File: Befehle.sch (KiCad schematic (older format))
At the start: 60 parts, among them J1 2PinTerminalBlocktg, J2 2PinTerminalBlocktg, J3 3PinTerminalBlocktg, J4 2PinTerminalBlocktg, J5 2PinTerminalBlocktg, P1 CONN_02X10, P2 CONN_02X10, U1 74LS14, U2 74540, U3 7400, U4 74HCT02, U5 74LS541, U6 74LS373, U7 74LS139, U8 74LS540

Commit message: wires gelegt und schamdoozels beseitigt
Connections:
- net labels added: d44, v1, v2
- net labels removed: 11, d0, d8
- wire segments 285 -> 289
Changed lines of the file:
@@
 d1
 Text Label -6300 4700 3    60   ~ 0
-d2
+d3
 Text Label -6400 4700 3    60   ~ 0
-d3
+d5
 Text Label -6500 4700 3    60   ~ 0
 d4
 Text Label -6600 4700 3    60   ~ 0
-d5
+d6
 Text Label -6700 4700 3    60   ~ 0
-d6
+d44
 Text Label -6800 4700 3    60   ~ 0
 d7
 Text Label -7100 4400 1    60   ~ 0
-d1
+d7
 Text Label -7100 4600 1    60   ~ 0
 d2
 Text Label -6950 5000 1    60   ~ 0
-d3
+d6
 Text Label -7050 5150 1    60   ~ 0
-d4
+d44
 Text Label -7100 5500 1    60   ~ 0
 d5
 Text Label -7100 5700 1    60   ~ 0
-d6
+d4
 Text Label -7100 6050 1    60   ~ 0
-d7
+d1
 Text Label -7100 6250 1    60   ~ 0
-d8
+d3
 Entry Wire Line
 	-5900 6800 -6000 6900
@@
 d1
 Text Label -6100 6900 1    60   ~ 0
-d2
+d7
 Text Label -6200 6900 1    60   ~ 0
 d3
 Text Label -6300 6900 1    60   ~ 0
-d4
+d44
 Text Label -6400 6900 1    60   ~ 0
 d5
@@
 d6
 Text Label -6600 6900 1    60   ~ 0
-d7
+d4
 Text Label -6200 550  1    60   ~ 0
 y1
@@
 	0    -1   -1   0
 $EndComp
-Text Label -6950 6250 0    60   ~ 0
-11
 Text Label -6900 4700 1    60   ~ 0
 d2
@@
 F 0 "D22" V 2841 6822 50  0000 R CNN
 F 1 "D" V 2750 6822 50  0000 R CNN
-F 2 "Diodes_ThroughHole:D_DO-41_SOD81_P10.16mm_Horizontal" V 2659 6822 50  0000 R CNN
+F 2 "Diodes_ThroughHole:D_DO-41_SOD81_P10.16mm_Horizontal" V 2650 6750 50  0000 R CNN
 F 3 "" H 2750 6900 50  0000 C CNN
 	1    2750 6900
@@
 Wire Wire Line
 	-8700 7850 -8700 8100
-Connection ~ -8700 7850
 Wire Wire Line
 	-9350 5350 -9150 5350
@@
 	37900 55900 37900 44500
 Wire Bus Line
-	37900 44500 50200 44500
-Wire Bus Line
-	50200 44500 50200 20050
-Wire Bus Line
-	50200 20050 65050 20050
-Wire Bus Line
-	65050 45000 77600 45000
-Wire Bus Line
 	77600 45000 77600 54250
 Wire Bus Line
 	77600 54250 77700 54250
-Wire Bus Line
-	65050 20050 65050 45000
-Wire Bus Line
-	56650 20400 56650 27200
-Wire Bus Line
-	64850 27200 64850 26900
-Wire Bus Line
-	50250 27200 56650 27200
-Connection ~ 56650 27200
 Wire Bus Line
 	-54500 -26200 -54500 -18100
@@
 	-3900 5450 -3900 6050
 Wire Wire Line
-	-8700 7850 -8200 7850
-Wire Wire Line
 	-9150 5350 -8650 5350
 Wire Wire Line
@@
 	-5450 -800 -5450 -550
 Wire Wire Line
-	-8300 5050 -8300 6650
-Wire Bus Line
-	56650 27200 64850 27200
+	-8300 5050 -8300 5600
 Wire Bus Line
 	-54500 -18100 -40100 -18100
@@
 Connection ~ -6500 3300
 Text Label -5900 6900 1    60   ~ 0
-d0
+d2
+Connection ~ -8300 5600
+Wire Wire Line
+	-8300 5600 -8300 6150
+Connection ~ -8300 6150
+Wire Wire Line
+	-8300 6150 -8300 6650
+Text Label -8650 6650 0    50   ~ 0
+v1
+Text Label -8400 7850 0    50   ~ 0
+v1
+Connection ~ -8700 7850
+Wire Wire Line
+	-8700 7850 -8400 7850
+Wire Wire Line
+	-8400 7850 -8200 7850
+Text Label -8400 7850 0    50   ~ 0
+v2
+Text Label -8750 5450 0    50   ~ 0
+v2
+Wire Wire Line
+	-8300 6650 -8500 6650
 Wire Bus Line
 	-6500 6800 -6300 6800
 Wire Bus Line
+	-4650 1950 -3950 1950
+Wire Bus Line
+	-6900 2650 -3950 2650
+Wire Bus Line
+	-6300 4850 -6300 6800
+Wire Bus Line
 	-6300 6800 -5800 6800
 Wire Bus Line
-	-4650 1950 -3950 1950
-Wire Bus Line
-	-6900 2650 -3950 2650
-Wire Bus Line
-	-6300 4850 -6300 6800
-Wire Bus Line
 	-7050 4850 -6300 4850
+Connection ~ -8300 6650
+Connection ~ -8500 6650
 $EndSCHEMATC

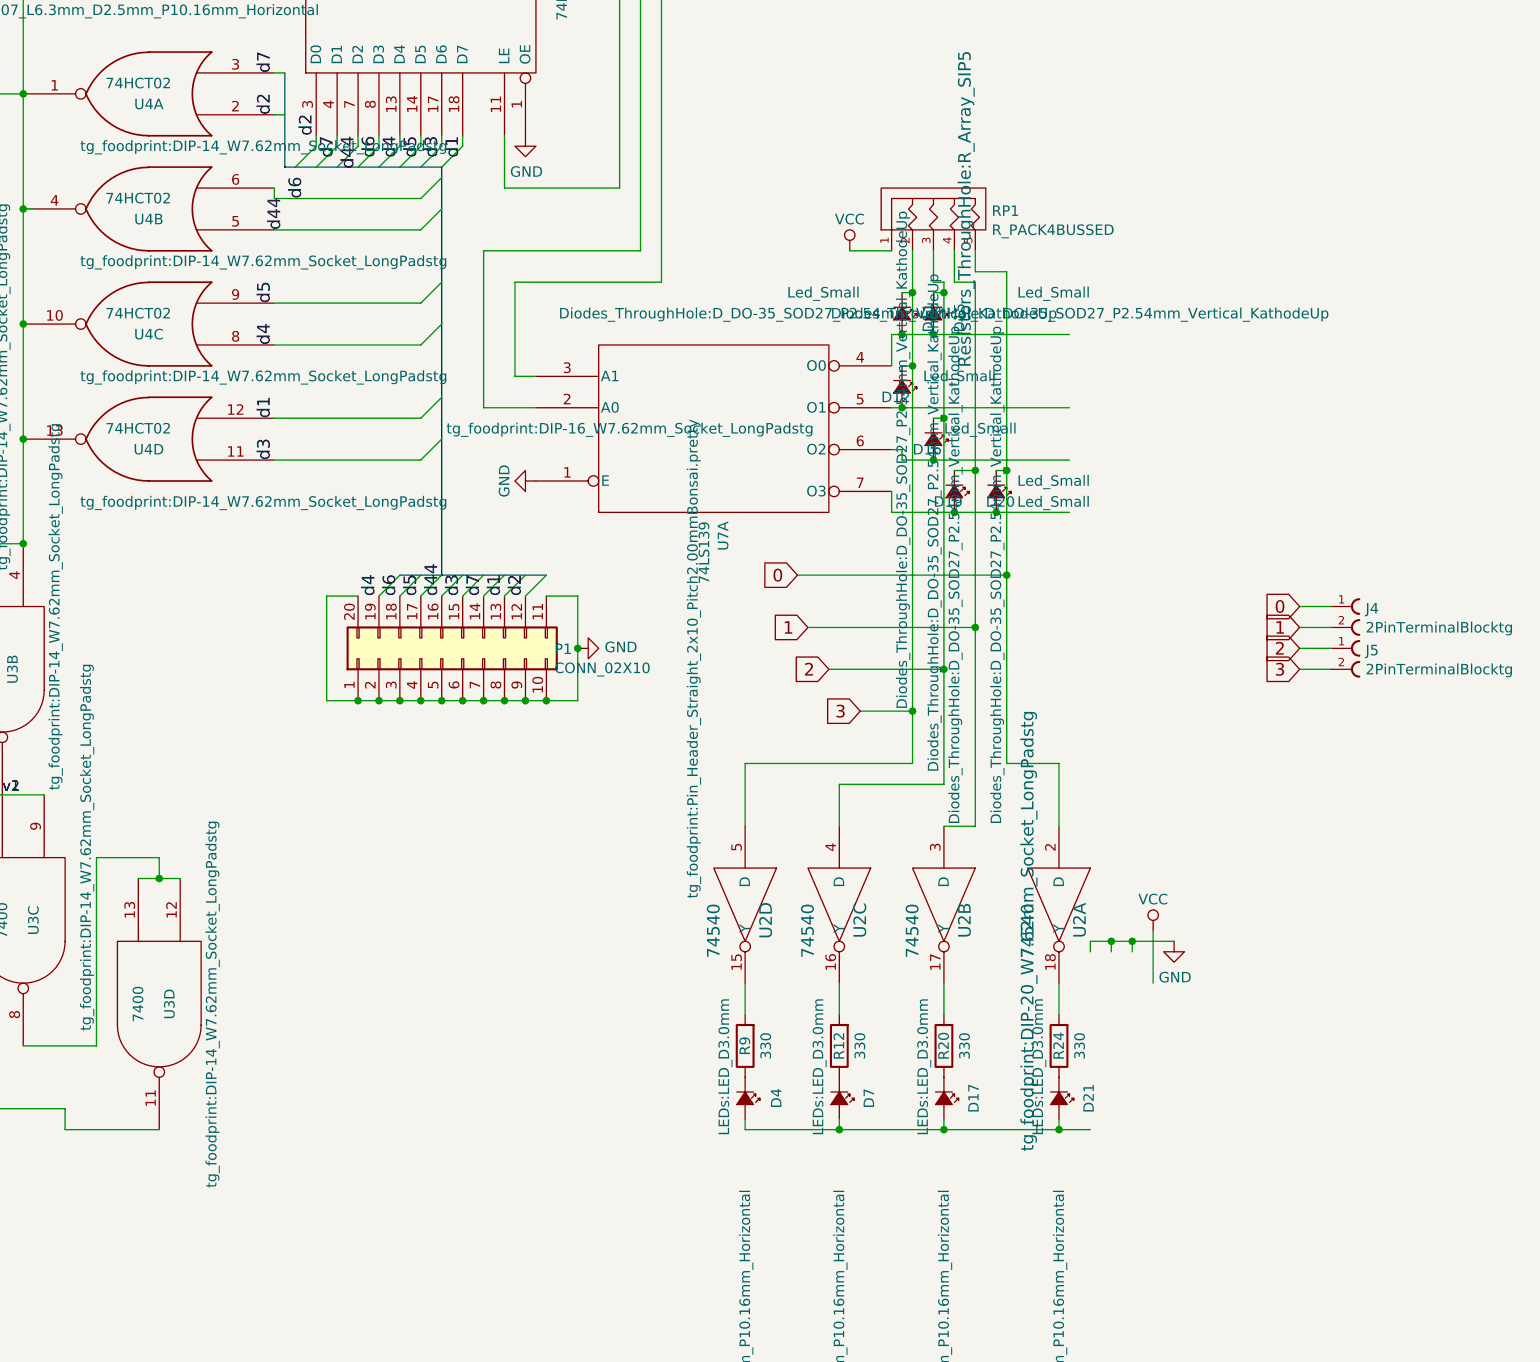
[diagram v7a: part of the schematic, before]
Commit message: wires gelegt footprints getauscht
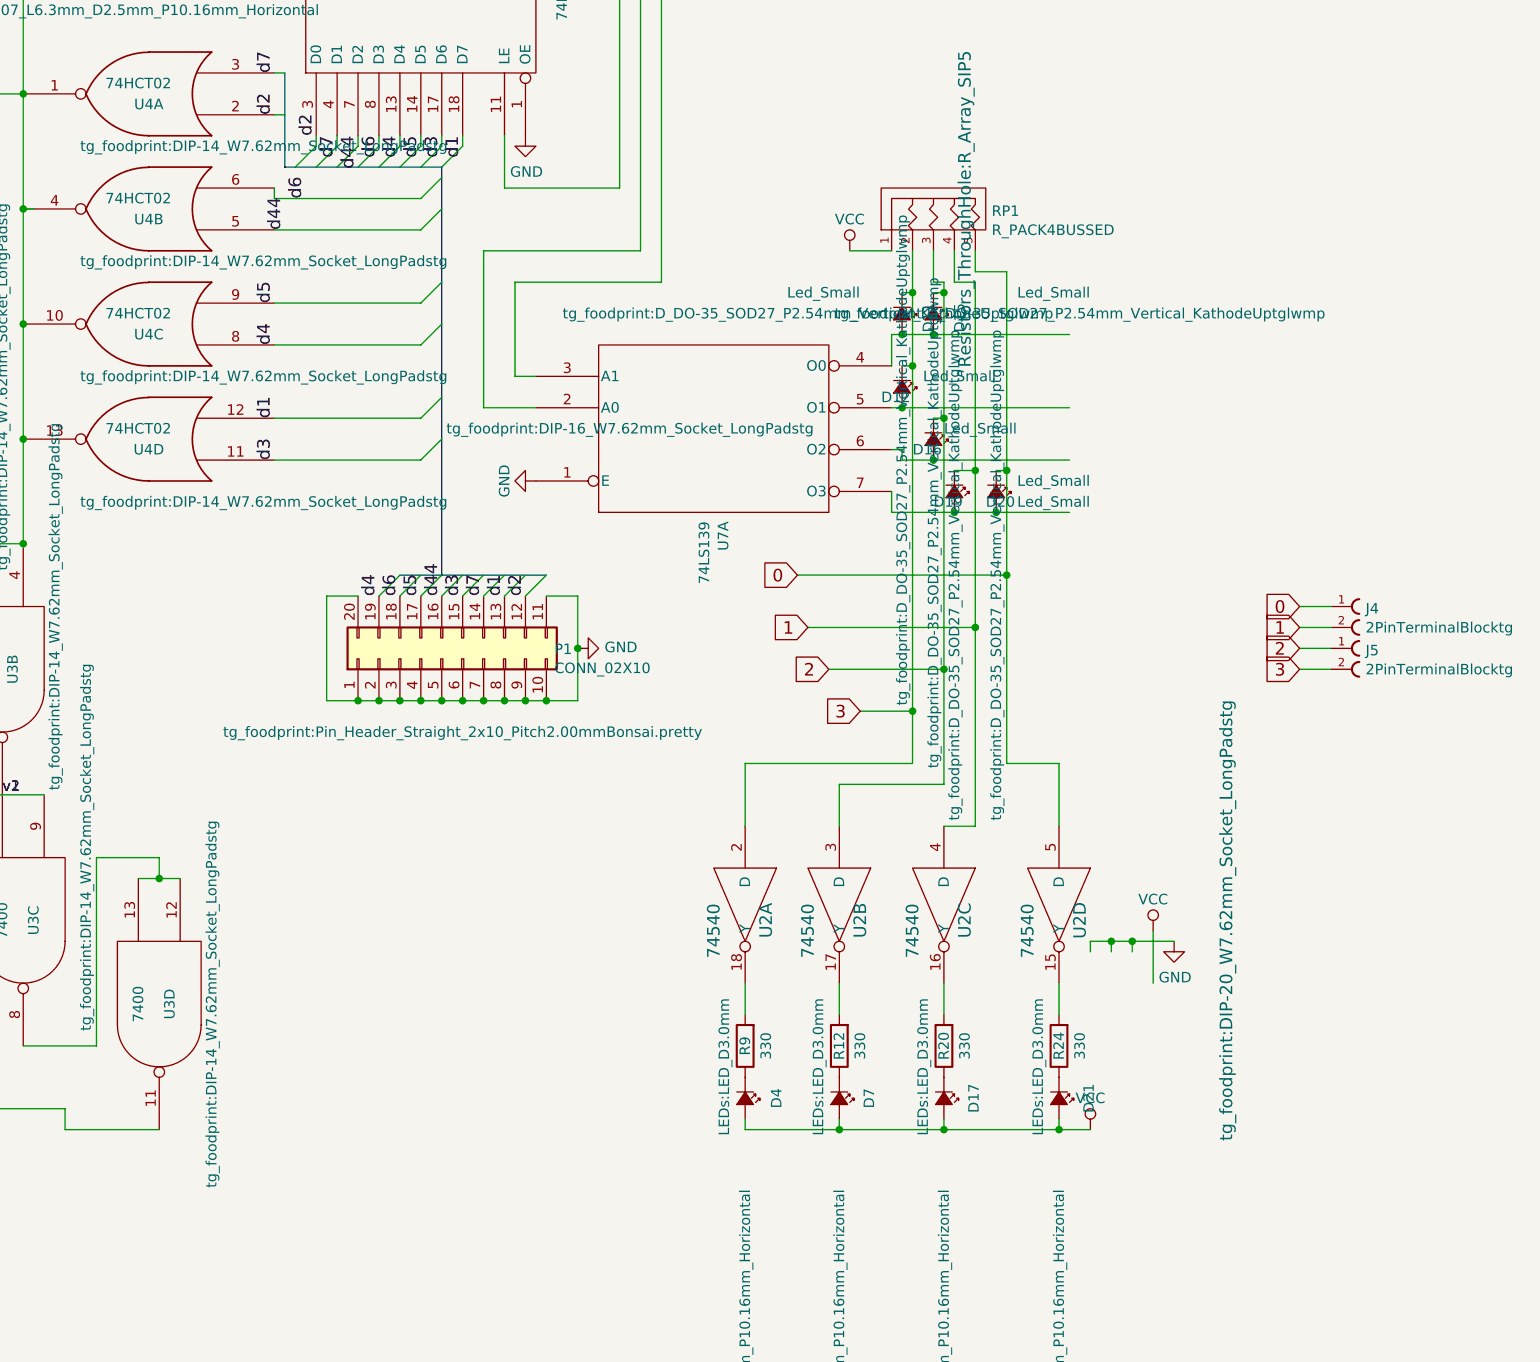
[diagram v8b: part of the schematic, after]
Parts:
- D11, D12, D15, D16, D19, D20: footprint Diodes_ThroughHole:D_DO-35_SOD27_P2.54mm_Vertical_KathodeUp -> tg_foodprint:D_DO-35_SOD27_P2.54mm_Vertical_KathodeUptglwmp
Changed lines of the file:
@@
 F 0 "D15" H -4000 5675 50  0000 L CNN
 F 1 "Led_Small" V -4050 5950 50  0000 L CNN
-F 2 "Diodes_ThroughHole:D_DO-35_SOD27_P2.54mm_Vertical_KathodeUp" V -3950 6250 50  0000 C CNN
+F 2 "tg_foodprint:D_DO-35_SOD27_P2.54mm_Vertical_KathodeUptglwmp" V -3950 6250 50  0000 C CNN
 F 3 "" V -3950 5550 50  0000 C CNN
 	1    -3950 5550
@@
 F 0 "D11" H -4150 5675 50  0000 L CNN
 F 1 "Led_Small" V -4200 5000 50  0000 L CNN
-F 2 "Diodes_ThroughHole:D_DO-35_SOD27_P2.54mm_Vertical_KathodeUp" V -4100 5100 50  0000 C CNN
+F 2 "tg_foodprint:D_DO-35_SOD27_P2.54mm_Vertical_KathodeUptglwmp" V -4100 5100 50  0000 C CNN
 F 3 "" V -4100 5550 50  0000 C CNN
 	1    -4100 5550
@@
 F 0 "D12" V -4050 5800 50  0000 L CNN
 F 1 "Led_Small" V -4150 6000 50  0000 L CNN
-F 2 "Diodes_ThroughHole:D_DO-35_SOD27_P2.54mm_Vertical_KathodeUp" H -3750 5900 50  0000 C CNN
+F 2 "tg_foodprint:D_DO-35_SOD27_P2.54mm_Vertical_KathodeUptglwmp" H -3750 5900 50  0000 C CNN
 F 3 "" V -4100 5900 50  0000 C CNN
 	1    -4100 5900
@@
 F 0 "D16" V -3900 6050 50  0000 L CNN
 F 1 "Led_Small" V -4000 6200 50  0000 L CNN
-F 2 "Diodes_ThroughHole:D_DO-35_SOD27_P2.54mm_Vertical_KathodeUp" H -3550 6150 50  0000 C CNN
+F 2 "tg_foodprint:D_DO-35_SOD27_P2.54mm_Vertical_KathodeUptglwmp" H -3550 6150 50  0000 C CNN
 F 3 "" V -3950 6150 50  0000 C CNN
 	1    -3950 6150
@@
 F 0 "D20" V -3600 6350 50  0000 L CNN
 F 1 "Led_Small" V -3700 6500 50  0000 L CNN
-F 2 "Diodes_ThroughHole:D_DO-35_SOD27_P2.54mm_Vertical_KathodeUp" H -3250 6400 50  0000 C CNN
+F 2 "tg_foodprint:D_DO-35_SOD27_P2.54mm_Vertical_KathodeUptglwmp" H -3250 6400 50  0000 C CNN
 F 3 "" V -3650 6400 50  0000 C CNN
 	1    -3650 6400
@@
 F 0 "D19" V -3800 6300 50  0000 L CNN
 F 1 "Led_Small" V -3800 6700 50  0000 L CNN
-F 2 "Diodes_ThroughHole:D_DO-35_SOD27_P2.54mm_Vertical_KathodeUp" H -3450 6400 50  0000 C CNN
+F 2 "tg_foodprint:D_DO-35_SOD27_P2.54mm_Vertical_KathodeUptglwmp" H -3450 6400 50  0000 C CNN
 F 3 "" V -3850 6400 50  0000 C CNN
 	1    -3850 6400
@@
 F 0 "P1" V -6254 6662 50  0000 R CNN
 F 1 "CONN_02X10" V -6345 6662 50  0000 R CNN
-F 2 "tg_foodprint:Pin_Header_Straight_2x10_Pitch2.00mmBonsai.pretty" H -6300 6000 50  0000 C CNN
+F 2 "tg_foodprint:Pin_Header_Straight_2x10_Pitch2.00mmBonsai.pretty" V -6650 7100 50  0000 C CNN
 F 3 "" H -6300 6000 50  0000 C CNN
 	1    -6300 7200
@@
 $Comp
 L 74540:74540 U2
-U 4 1 5A28303B
+U 1 1 5A28303B
 P -4850 8350
 F 0 "U2" H -4750 8450 60  0000 C CNN
@@
 F 2 "tg_foodprint:DIP-20_W7.62mm_Socket_LongPadstg" H -4700 8200 60  0001 C CNN
 F 3 "" H -4700 8200 60  0001 C CNN
-	4    -4850 8350
+	1    -4850 8350
 	0    1    1    0
 $EndComp
 $Comp
 L 74540:74540 U2
-U 3 1 5A282F54
+U 2 1 5A282F54
 P -4400 8350
 F 0 "U2" H -4300 8450 60  0000 C CNN
@@
 F 2 "tg_foodprint:DIP-20_W7.62mm_Socket_LongPadstg" H -4250 8200 60  0001 C CNN
 F 3 "" H -4250 8200 60  0001 C CNN
-	3    -4400 8350
+	2    -4400 8350
 	0    1    1    0
 $EndComp
 $Comp
 L 74540:74540 U2
-U 2 1 5A282E5F
+U 3 1 5A282E5F
 P -3900 8350
 F 0 "U2" H -3800 8450 60  0000 C CNN
@@
 F 2 "Housings_DIP:DIP-20_W7.62mm_Socket_LongPads" H -3750 8200 60  0001 C CNN
 F 3 "" H -3750 8200 60  0001 C CNN
-	2    -3900 8350
+	3    -3900 8350
 	0    1    1    0
 $EndComp
 $Comp
 L 74540:74540 U2
-U 1 1 5A282C7C
+U 4 1 5A282C7C
 P -3350 8350
 F 0 "U2" H -3250 8450 60  0000 C CNN
 F 1 "74540" H -3200 8200 60  0000 C CNN
-F 2 "tg_foodprint:DIP-20_W7.62mm_Socket_LongPadstg" H -3200 8200 60  0000 C CNN
+F 2 "tg_foodprint:DIP-20_W7.62mm_Socket_LongPadstg" H -3250 9150 60  0000 C CNN
 F 3 "" H -3200 8200 60  0001 C CNN
-	1    -3350 8350
+	4    -3350 8350
 	0    1    1    0
 $EndComp
@@
 Wire Wire Line
 	-8300 6650 -8500 6650
-Wire Bus Line
-	-6500 6800 -6300 6800
-Wire Bus Line
-	-4650 1950 -3950 1950
-Wire Bus Line
-	-6900 2650 -3950 2650
-Wire Bus Line
-	-6300 4850 -6300 6800
-Wire Bus Line
-	-6300 6800 -5800 6800
-Wire Bus Line
-	-7050 4850 -6300 4850
 Connection ~ -8300 6650
 Connection ~ -8500 6650
+$Comp
+L power:VCC #PWR019
+U 1 1 5AF5D5F2
+P -3200 9450
+F 0 "#PWR019" H -3200 9300 50  0001 C CNN
+F 1 "VCC" H -3200 9600 50  0000 C CNN
+F 2 "" H -3200 9450 50  0000 C CNN
+F 3 "" H -3200 9450 50  0000 C CNN
+	1    -3200 9450
+	1    0    0    -1
+$EndComp
+Wire Bus Line
+	-6500 6800 -6300 6800
+Wire Bus Line
+	-4650 1950 -3950 1950
+Wire Bus Line
+	-6900 2650 -3950 2650
+Wire Bus Line
+	-6300 4850 -6300 6800
+Wire Bus Line
+	-6300 6800 -5800 6800
+Wire Bus Line
+	-7050 4850 -6300 4850
 $EndSCHEMATC
